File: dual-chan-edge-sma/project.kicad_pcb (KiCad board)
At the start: 2 copper layers, 39 x 27.2 mm, 16 parts, among them J1 Conn_01x08_Female, J2 Conn_01x08_Female, J3 Conn_01x02_Female, J4 Conn_01x04_Male, J5 Conn_01x08_Female, J6 Conn_01x08_Female, J8 Conn_01x04_Male, J9 Conn_01x05_Male

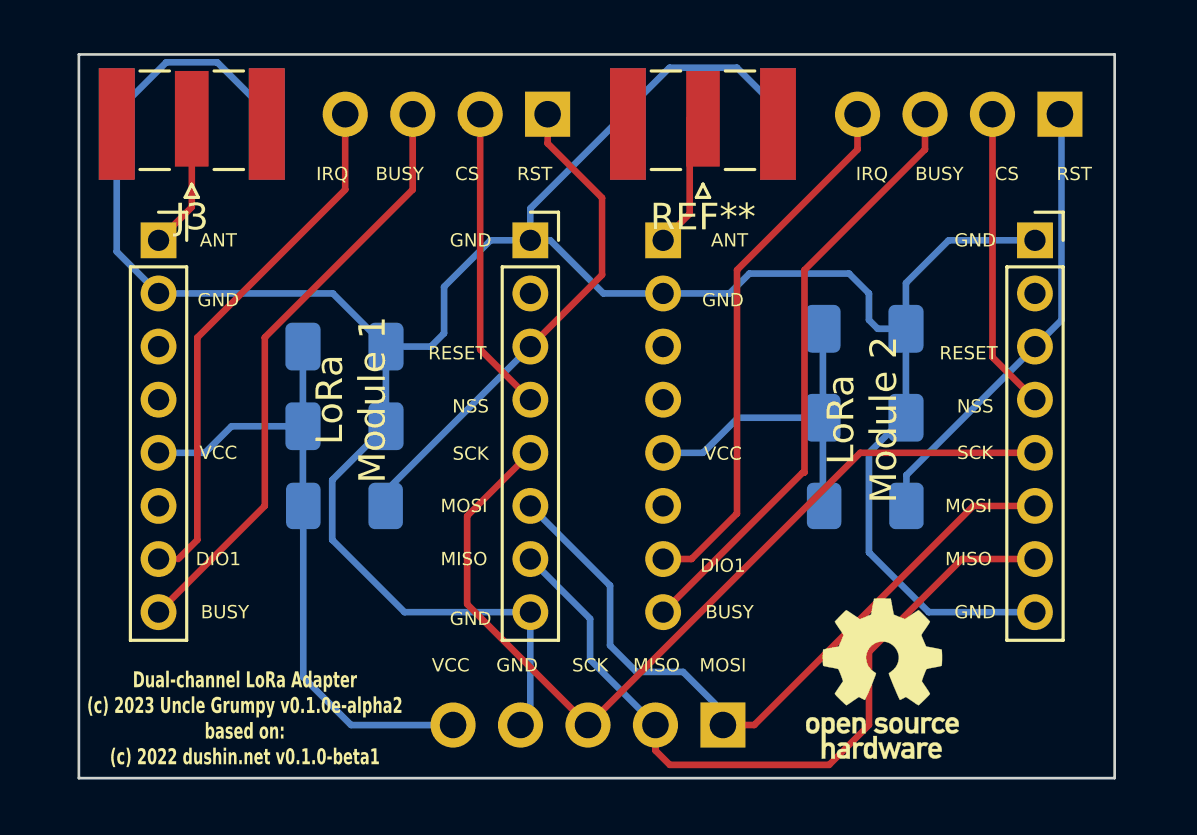
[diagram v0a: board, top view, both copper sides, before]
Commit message: Version 0.1.0e-alpha3
Moves the SMA connectords to opposite sides of the board and flips LoRa module 2
180 degrees. Silkscreen lettering flipped on module 2 to give better visual
indication of orientation.

Signed-off-by: Winford <winford@object.stream>
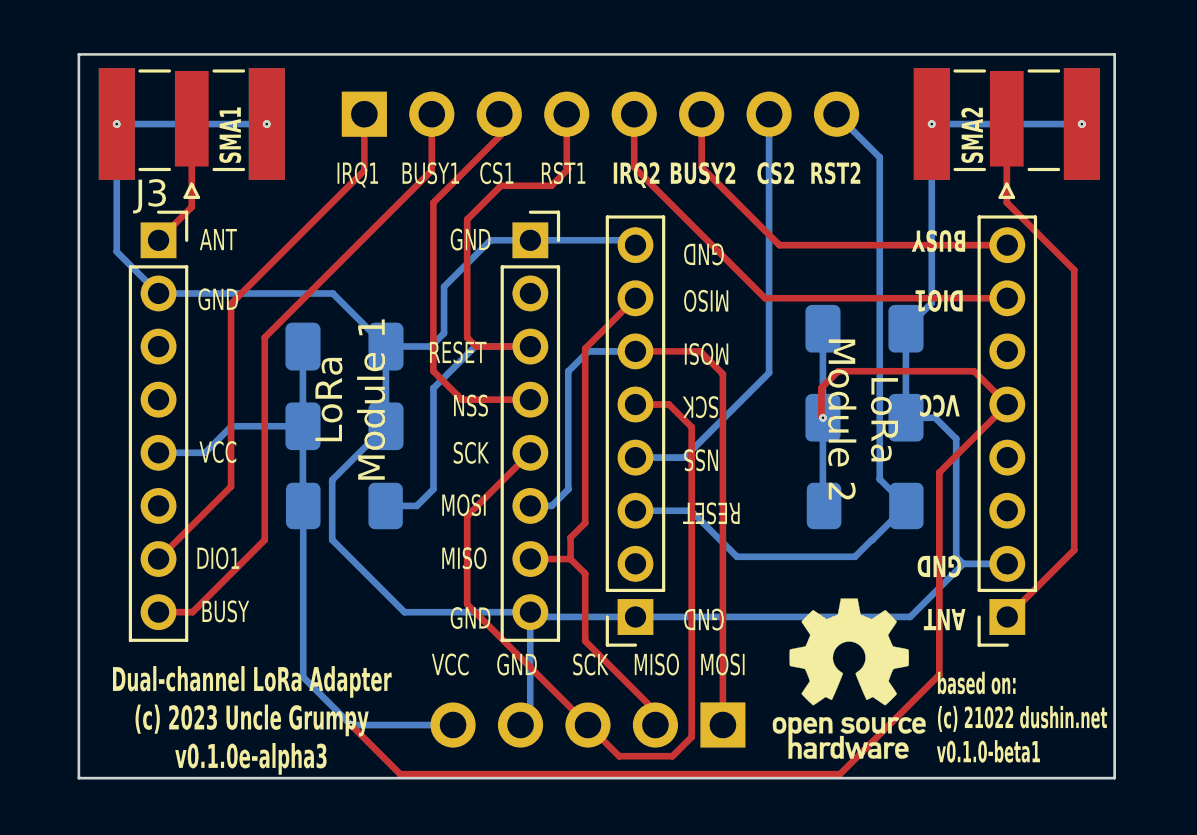
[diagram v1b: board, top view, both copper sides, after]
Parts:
- removed J8: Conn_01x04_Male, Connector_PinHeader_2.54mm:PinHeader_1x04_P2.54mm_Vertical
- J4: footprint Connector_PinHeader_2.54mm:PinHeader_1x04_P2.54mm_Vertical -> Connector_PinHeader_2.54mm:PinHeader_1x08_P2.54mm_Vertical
- J5: moved to F.Cu
- moved J6 20.7 mm to (141.0, 84.2), turned to 180 degrees
- moved J5 19.2 mm to (155.0, 84.2)
- moved SMA2 11.4 mm to (154.9, 65.6)
- moved J4 6.90 mm to (130.8, 65.2), turned to -90 degrees
- moved REF** 1.25 mm to (149.0, 86.5)
- renumbered REF** to SMA2
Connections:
- J4 pad 1: /RESET1 -> /IRQ1
- J4 pad 2: /CS1 -> /BUSY1
- J4 pad 3: /BUSY1 -> /CS1
- J4 pad 4: /IRQ1 -> /RESET1
- SMA2 pad 2: /ANT2 -> /GND
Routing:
- net /VCC: track 37.9 -> 75.9 mm, vias 0 -> 2
- net /ANT2: track 4.99 -> 20.9 mm
- net /RESET2: track 17.2 -> 27.6 mm
- net /GND: track 106.8 -> 97.3 mm, vias 0 -> 4
- net /MISO: track 28.5 -> 19.4 mm
- net /BUSY2: track 23.2 -> 14.7 mm
- net /RESET1: track 19.0 -> 23.8 mm
- net /CS2: track 11.4 -> 16.1 mm
- net /CS1: track 11.5 -> 14.9 mm
- net /IRQ2: track 20.4 -> 18.1 mm
- net /SCK: track 34.2 -> 31.9 mm
- net /MOSI: track 27.4 -> 25.8 mm
- net /BUSY1: track 22.7 -> 23.8 mm
- net /IRQ1: track 19.4 -> 20.0 mm
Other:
- board text added: "BUSY1"
- board text added: "BUSY2"
- board text added: "CS1"
- board text added: "CS2"
- board text added: "Dual-channel LoRa Adapter (c) 2023 Uncle Grumpy v0.1.0e-alpha3"
- board text added: "IRQ1"
- board text added: "IRQ2"
- board text added: "RST1"
- board text added: "RST2"
- board text added: "RTS2"
- board text added: "SMA1"
- board text added: "based on: (c) 21022 dushin.net v0.1.0-beta1"
- board text removed: "CS"
- board text removed: "Dual-channel LoRa Adapter (c) 2023 Uncle Grumpy v0.1.0e-alpha2 based on: (c) 2022 dushin.net v0.1.0-beta1"
- board text removed: "IRQ"
- board text removed: "RST"
